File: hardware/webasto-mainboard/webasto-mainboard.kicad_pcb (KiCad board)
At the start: 4 copper layers, 86.8 x 76 mm, 91 parts, among them J1 Console FTDI, J2 DEBUG, J3 2-pole connector, Q1 DMG2301L, Q10 DMG2301L, Q11 SSM3J374R, Q12 2N7002, Q13 SUD50P04-08, Q14 SUD50P04-08, Q15 SUD50P04-08, Q16 SUD50P04-08, Q17 SUD50P04-08, Q18 2N7002, Q19 2N7002, Q2 2N7002, Q3 2N7002, Q4 2N7002, Q5 2N7002, Q6 SUD50P04-08, Q7 SUD50P04-08, Q8 SUD50P04-08, Q9 SUD50P04-08, U1 CY15E004J, U2 Pico, U3 LM4040DBZ-2.0, U4 MC33660BEFR2, U5 BD9G341EFJ, U6 LM7805_TO220, U7 INA219BxDCN

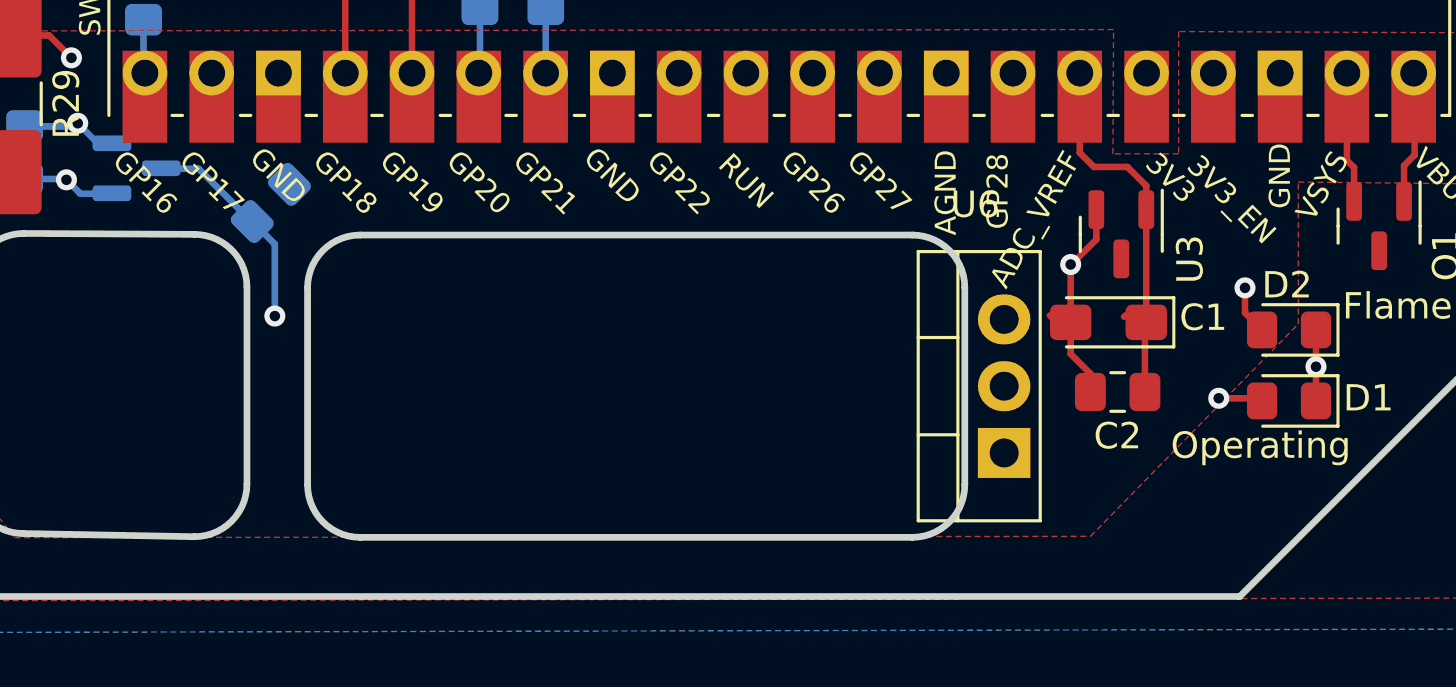
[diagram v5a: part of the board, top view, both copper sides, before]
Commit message: Tweak routes to not go along bottom edge
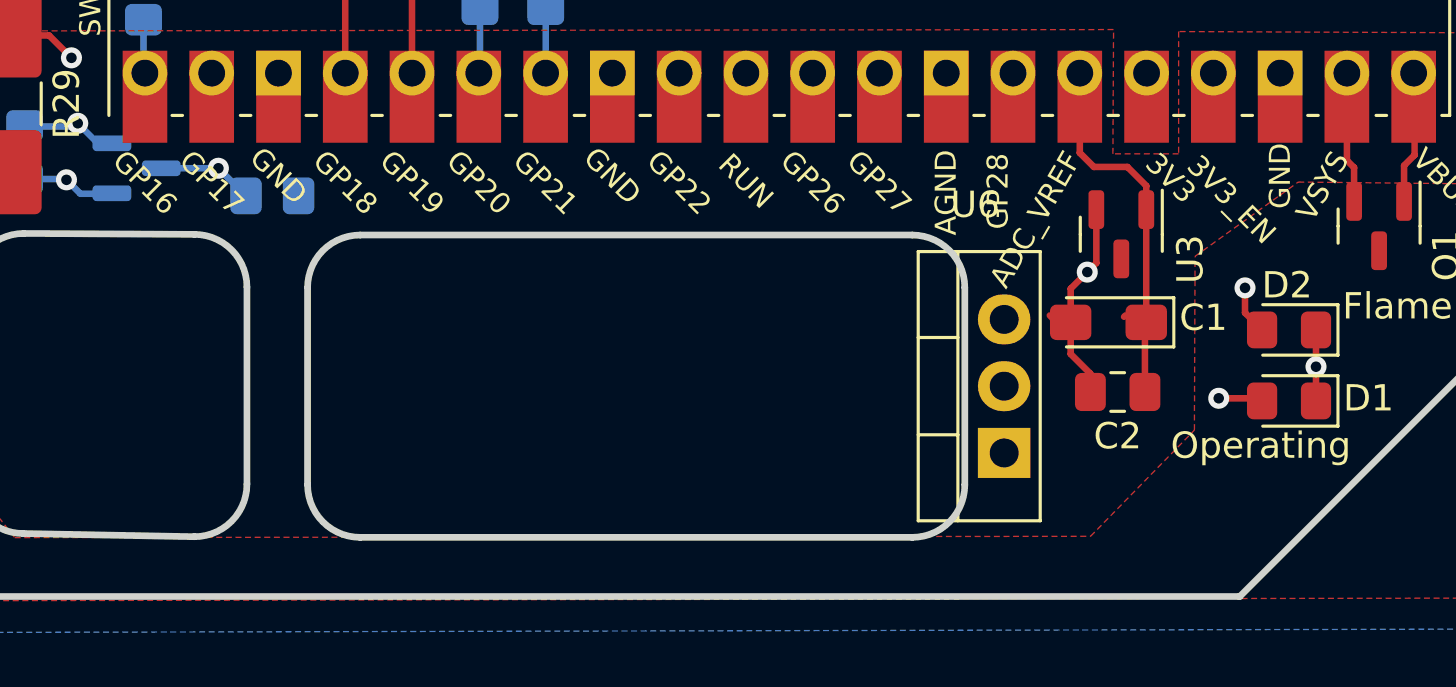
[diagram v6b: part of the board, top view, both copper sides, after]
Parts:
- moved R27 0.28 mm to (141.0, 114.3), turned to 0 degrees
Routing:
- net Net-(Q11-Pad3): track 48.1 -> 45.7 mm
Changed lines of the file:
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@@
   (paper "USLetter")
   (title_block
-    (title "Webasto Replacement Mainboard (Therma Top C)")
+    (title "Webasto Replacement Mainboard (Thermo Top C)")
     (date "2023-01-18")
     (rev "1.0")
@@
   )
   (footprint "Resistor_SMD:R_0805_2012Metric_Pad1.20x1.40mm_HandSolder" (layer "B.Cu")
-    (at 140.945647 114.569788 45)
+    (at 141 114.3)
     (descr "Resistor SMD 0805 (2012 Metric), square (rectangular) end terminal, IPC_7351 nominal with elongated pad for handsoldering. (Body size source: IPC-SM-782 page 72, https://www.pcb-3d.com/wordpress/wp-content/uploads/ipc-sm-782a_amendment_1_and_2.pdf), generated with kicad-footprint-generator")
     (tags "resistor handsolder")
@@
     (property "Sheetname" "Glow Plug")
     (attr smd)
-    (fp_text reference "R27" (at 0 1.65 45) (layer "B.SilkS")
+    (fp_text reference "R27" (at 0 1.65) (layer "B.SilkS")
       (effects (font (size 1 1) (thickness 0.15)) (justify mirror))
     )
-    (fp_text value "10k" (at 0 -1.65 45) (layer "B.Fab")
+    (fp_text value "10k" (at 0 -1.65) (layer "B.Fab")
       (effects (font (size 1 1) (thickness 0.15)) (justify mirror))
     )
-    (fp_text user "${REFERENCE}" (at 0 0 45) (layer "B.Fab")
+    (fp_text user "${REFERENCE}" (at 0 0) (layer "B.Fab")
       (effects (font (size 0.5 0.5) (thickness 0.08)) (justify mirror))
     )
@@
     (fp_line (start -1 -0.625) (end -1 0.625) (layer "B.Fab") (width 0.1))
     (fp_line (start 1 -0.625) (end -1 -0.625) (layer "B.Fab") (width 0.1))
-    (pad "1" smd roundrect (at -1 0 45) (size 1.2 1.4) (layers "B.Cu" "B.Paste" "B.Mask") (roundrect_rratio 0.208333)
+    (pad "1" smd roundrect (at -1 0) (size 1.2 1.4) (layers "B.Cu" "B.Paste" "B.Mask") (roundrect_rratio 0.208333)
       (net 56 "Net-(Q11-Pad3)") (pintype "passive"))
-    (pad "2" smd roundrect (at 1 0 45) (size 1.2 1.4) (layers "B.Cu" "B.Paste" "B.Mask") (roundrect_rratio 0.208333)
+    (pad "2" smd roundrect (at 1 0) (size 1.2 1.4) (layers "B.Cu" "B.Paste" "B.Mask") (roundrect_rratio 0.208333)
       (net 30 "GND") (pintype "passive"))
     (model "${KICAD6_3DMODEL_DIR}/Resistor_SMD.3dshapes/R_0805_2012Metric.wrl"
@@
   (segment (start 172.119 121.76075) (end 172.119 121.065) (width 0.25) (layer "F.Cu") (net 30))
   (segment (start 139.250303 75.02148) (end 139.250303 76.381311) (width 0.25) (layer "F.Cu") (net 30))
+  (segment (start 171.369 117.831) (end 172 117.2) (width 0.25) (layer "F.Cu") (net 30))
   (segment (start 145.161 85.979) (end 144.526 86.614) (width 0.25) (layer "F.Cu") (net 30))
   (segment (start 172.119 121.065) (end 171.369 120.315) (width 0.25) (layer "F.Cu") (net 30))
+  (segment (start 172.344 116.856) (end 172.344 114.82325) (width 0.25) (layer "F.Cu") (net 30))
   (segment (start 107.125 106.3) (end 108.025 107.2) (width 0.25) (layer "F.Cu") (net 30))
   (segment (start 147.701 85.134) (end 146.431 85.134) (width 0.25) (layer "F.Cu") (net 30))
-  (segment (start 172.344 115.96075) (end 171.494 116.81075) (width 0.25) (layer "F.Cu") (net 30))
   (segment (start 102.025 105.675) (end 101.725 105.375) (width 0.25) (layer "F.Cu") (net 30))
-  (segment (start 172.344 114.82325) (end 172.344 115.96075) (width 0.25) (layer "F.Cu") (net 30))
   (segment (start 162.83 78.68) (end 162.83 78.115) (width 0.25) (layer "F.Cu") (net 30))
   (segment (start 108.95 106.175) (end 108.975 106.2) (width 0.25) (layer "F.Cu") (net 30))
   (segment (start 108.51 110.95) (end 107.875 110.315) (width 0.25) (layer "F.Cu") (net 30))
-  (segment (start 171.494 116.81075) (end 171.469 116.81075) (width 0.25) (layer "F.Cu") (net 30))
   (segment (start 117.6 111.7) (end 118.6 111.7) (width 0.25) (layer "F.Cu") (net 30))
   (segment (start 118.6 111.7) (end 119.025 112.125) (width 0.25) (layer "F.Cu") (net 30))
@@
   (segment (start 125.475 125.95) (end 125.475 127.175) (width 0.25) (layer "F.Cu") (net 30))
   (segment (start 140.46 74.46) (end 139.811783 74.46) (width 0.25) (layer "F.Cu") (net 30))
+  (segment (start 172 117.2) (end 172.344 116.856) (width 0.25) (layer "F.Cu") (net 30))
   (segment (start 107.125 106.175) (end 107.125 106.3) (width 0.25) (layer "F.Cu") (net 30))
   (segment (start 131.025 100.74) (end 136.385 100.74) (width 0.25) (layer "F.Cu") (net 30))
   (segment (start 180.7 122.1) (end 180.7 119.4) (width 0.25) (layer "F.Cu") (net 30))
   (segment (start 145.161 77.934) (end 145.161 79.375) (width 0.25) (layer "F.Cu") (net 30))
+  (segment (start 171.369 119.11075) (end 171.369 117.831) (width 0.25) (layer "F.Cu") (net 30))
   (segment (start 125.475 127.175) (end 125.5 127.2) (width 0.25) (layer "F.Cu") (net 30))
   (segment (start 123.1125 106.8875) (end 123.5 106.5) (width 0.25) (layer "F.Cu") (net 30))
@@
   (segment (start 139.811783 74.46) (end 139.250303 75.02148) (width 0.25) (layer "F.Cu") (net 30))
   (segment (start 129.16 69.32) (end 129.16 66.41) (width 0.25) (layer "F.Cu") (net 30))
-  (segment (start 171.369 119.11075) (end 171.369 116.91075) (width 0.25) (layer "F.Cu") (net 30))
   (segment (start 128.9 66.15) (end 128.9 63.775) (width 0.25) (layer "F.Cu") (net 30))
   (segment (start 154.665 71.405) (end 154.665 67.215) (width 2) (layer "F.Cu") (net 30))
   (segment (start 145.161 79.375) (end 145.034 79.502) (width 0.25) (layer "F.Cu") (net 30))
-  (segment (start 171.469 116.81075) (end 171.369 116.91075) (width 0.25) (layer "F.Cu") (net 30))
   (via (at 144.526 86.614) (size 0.8) (drill 0.4) (layers "F.Cu" "B.Cu") (net 30))
   (via (at 101.725 105.375) (size 0.8) (drill 0.4) (layers "F.Cu" "B.Cu") (net 30))
@@
   (via (at 145.034 79.502) (size 0.8) (drill 0.4) (layers "F.Cu" "B.Cu") (net 30))
   (via (at 108.025 107.2) (size 0.8) (drill 0.4) (layers "F.Cu" "B.Cu") (net 30))
-  (via (at 171.369 116.91075) (size 0.8) (drill 0.4) (layers "F.Cu" "B.Cu") (net 30))
+  (via (at 172 117.2) (size 0.8) (drill 0.4) (layers "F.Cu" "B.Cu") (net 30))
   (via (at 119.025 112.125) (size 0.8) (drill 0.4) (layers "F.Cu" "B.Cu") (net 30))
   (via (at 154.66 67.21) (size 0.8) (drill 0.4) (layers "F.Cu" "B.Cu") (net 30))
@@
   (via (at 177 122) (size 0.8) (drill 0.4) (layers "F.Cu" "B.Cu") (net 55))
   (via (at 151.4 103.5) (size 0.8) (drill 0.4) (layers "F.Cu" "B.Cu") (net 55))
-  (segment (start 151.4 103.5) (end 152.4 103.5) (width 0.25) (layer "In1.Cu") (net 55))
-  (segment (start 157.734848 108.834848) (end 157.734848 111.134848) (width 0.25) (layer "In1.Cu") (net 55))
-  (segment (start 160 113.4) (end 169.6 113.4) (width 0.25) (layer "In1.Cu") (net 55))
-  (segment (start 157.734848 111.134848) (end 160 113.4) (width 0.25) (layer "In1.Cu") (net 55))
-  (segment (start 169.6 113.4) (end 177 120.8) (width 0.25) (layer "In1.Cu") (net 55))
   (segment (start 152.4 103.5) (end 157.734848 108.834848) (width 0.25) (layer "In1.Cu") (net 55))
+  (segment (start 151.4 103.5) (end 152.4 103.5) (width 0.25) (layer "In1.Cu") (net 55))
   (segment (start 177 120.8) (end 177 122) (width 0.25) (layer "In1.Cu") (net 55))
+  (segment (start 158.9 112.4) (end 168.6 112.4) (width 0.25) (layer "In1.Cu") (net 55))
+  (segment (start 157.734848 108.834848) (end 157.734848 111.234848) (width 0.25) (layer "In1.Cu") (net 55))
+  (segment (start 157.734848 111.234848) (end 158.9 112.4) (width 0.25) (layer "In1.Cu") (net 55))
+  (segment (start 168.6 112.4) (end 177 120.8) (width 0.25) (layer "In1.Cu") (net 55))
   (segment (start 151.4 105.2) (end 151.4 103.5) (width 0.25) (layer "B.Cu") (net 55))
-  (via (at 141.097 118.872) (size 0.8) (drill 0.4) (layers "F.Cu" "B.Cu") (net 56))
-  (segment (start 166.751 128.397) (end 168.839 126.309) (width 0.25) (layer "In1.Cu") (net 56))
-  (segment (start 141.986 128.397) (end 166.751 128.397) (width 0.25) (layer "In1.Cu") (net 56))
-  (segment (start 168.839 126.309) (end 168.839 124.079) (width 0.25) (layer "In1.Cu") (net 56))
-  (segment (start 141.097 127.508) (end 141.986 128.397) (width 0.25) (layer "In1.Cu") (net 56))
-  (segment (start 141.097 118.872) (end 141.097 127.508) (width 0.25) (layer "In1.Cu") (net 56))
-  (segment (start 140.23 115.3) (end 138.2 113.27) (width 0.25) (layer "B.Cu") (net 56))
-  (segment (start 140.23854 115.276895) (end 141.097 116.135355) (width 0.25) (layer "B.Cu") (net 56))
-  (segment (start 138.2 113.27) (end 136.7675 113.27) (width 0.25) (layer "B.Cu") (net 56))
-  (segment (start 141.097 116.135355) (end 141.097 118.872) (width 0.25) (layer "B.Cu") (net 56))
+  (via (at 138.95 113.25) (size 0.8) (drill 0.4) (layers "F.Cu" "B.Cu") (net 56))
+  (segment (start 138.95048 113.24952) (end 167.94952 113.24952) (width 0.25) (layer "In1.Cu") (net 56))
+  (segment (start 138.95 113.25) (end 138.95048 113.24952) (width 0.25) (layer "In1.Cu") (net 56))
+  (segment (start 171.1 116.4) (end 171.1 121.818) (width 0.25) (layer "In1.Cu") (net 56))
+  (segment (start 167.94952 113.24952) (end 171.1 116.4) (width 0.25) (layer "In1.Cu") (net 56))
+  (segment (start 171.1 121.818) (end 168.839 124.079) (width 0.25) (layer "In1.Cu") (net 56))
+  (segment (start 138.95 113.25) (end 140 114.3) (width 0.25) (layer "B.Cu") (net 56))
+  (segment (start 136.775 113.25) (end 138.95 113.25) (width 0.25) (layer "B.Cu") (net 56))
   (segment (start 176.9 91.745) (end 176.795 91.85) (width 0.25) (layer "In1.Cu") (net 57))
   (segment (start 177.3705 94.0585) (end 177.8 94.488) (width 0.25) (layer "B.Cu") (net 57))
@@
         (xy 131.2 127.3)
         (xy 172.125 127.25)
-        (xy 180.025 119.175)
+        (xy 176.075 123.2125)
+        (xy 176.1 116.6)
         (xy 180.025 113.775)
         (xy 187.35 113.85)

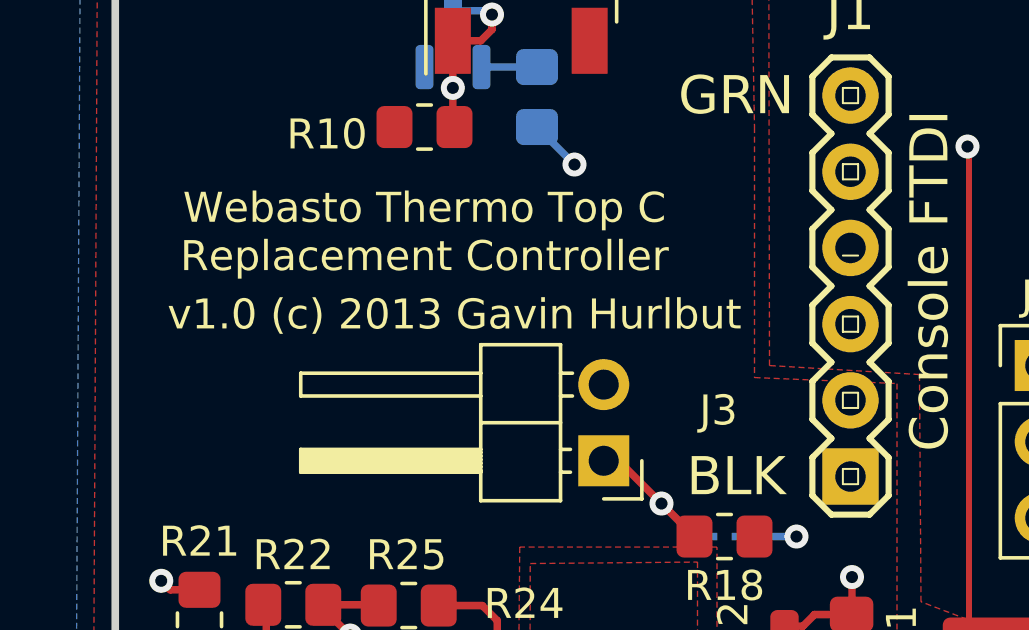
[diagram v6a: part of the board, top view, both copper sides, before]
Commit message: Fix copyright date.  2013?!!?
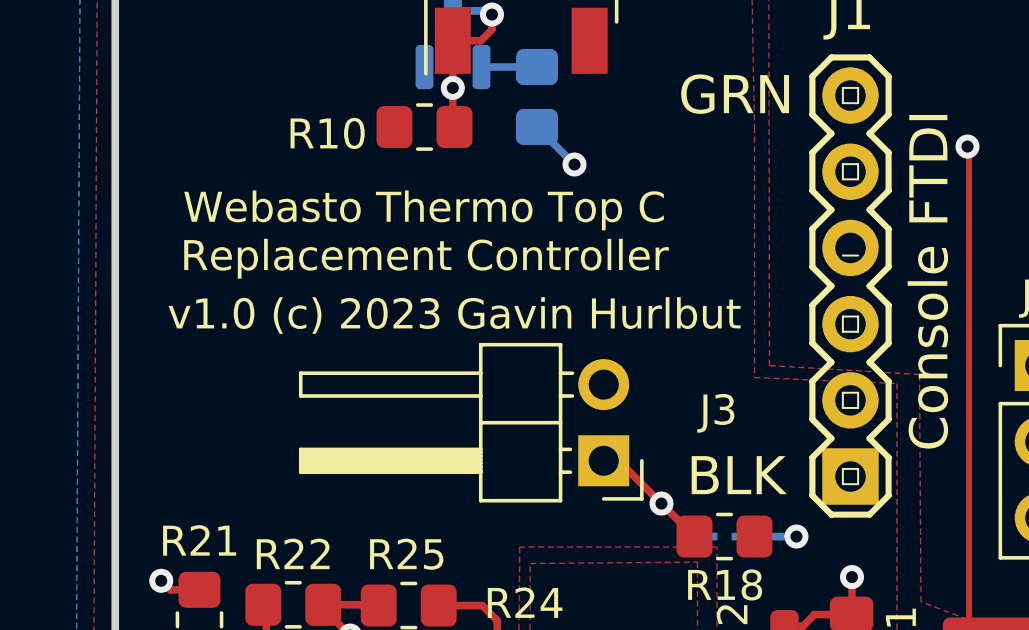
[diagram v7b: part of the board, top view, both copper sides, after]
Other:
- board text added: "v1.0 (c) 2023 Gavin Hurlbut"
- board text removed: "v1.0 (c) 2013 Gavin Hurlbut"
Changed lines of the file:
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@@
   (gr_line locked (start 129.514 117.695) (end 129.514 125.195) (layer "Edge.Cuts") (width 0.254))
   (gr_line locked (start 100.192 120.348) (end 109.384 129.54) (layer "Edge.Cuts") (width 0.254))
-  (gr_text "v1.0 (c) 2013 Gavin Hurlbut" (at 111.5 96.5) (layer "F.SilkS")
+  (gr_text "v1.0 (c) 2023 Gavin Hurlbut" (at 111.5 96.5) (layer "F.SilkS")
     (effects (font (size 1 1) (thickness 0.15)))
   )

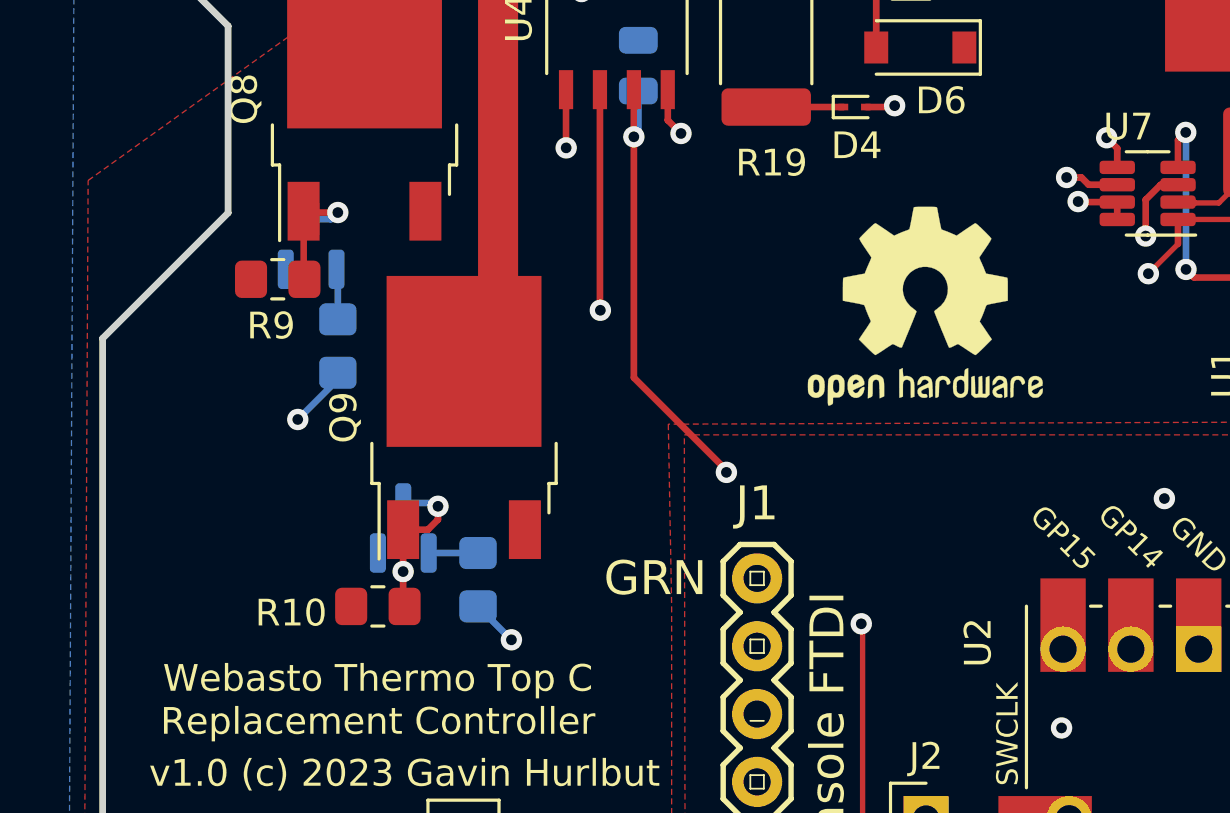
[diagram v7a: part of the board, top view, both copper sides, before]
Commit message: Filled out most of the rest (all?) of the FSM
- added a piezo for alarms  (like overheat!)
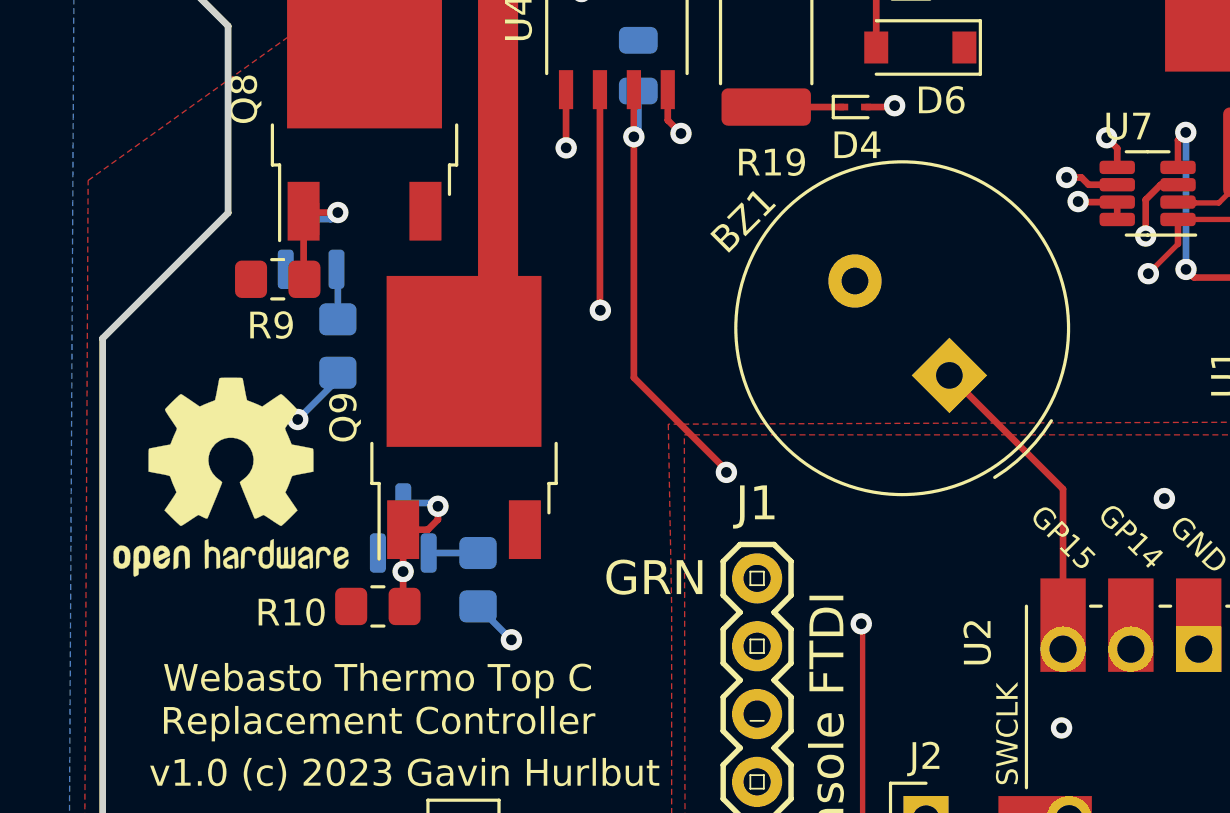
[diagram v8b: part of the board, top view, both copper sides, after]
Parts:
- added BZ1: Buzzer, Buzzer_Beeper:Buzzer_TDK_PS1240P02BT_D12.2mm_H6.5mm, F.Cu at (131.9, 81.6)
- moved REF** 26.8 mm to (105.0, 85.4)
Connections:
- U2 pad 20: unconnected-(U2-Pad20) -> ALERT
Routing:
- net ALERT: track 0.00 -> 12.0 mm
